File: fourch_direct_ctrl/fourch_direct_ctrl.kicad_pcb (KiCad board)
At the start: 4 copper layers, 72 x 72 mm, 53 parts, among them J1 Conn_01x04, J10 Conn_01x01, J11 Conn_01x01, J12 Conn_01x01, J13 Conn_01x01, J14 Conn_01x01, J15 Conn_01x01, J16 Conn_01x01, J17 Conn_01x01, J2 Conn_01x02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

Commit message: update silk
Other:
- board text added: "048ef97"
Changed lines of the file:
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@@
 		(layer "Edge.Cuts")
+	)
+	(gr_text "048ef97"
+		(at -35.5 3.5 -90)
+		(layer "F.SilkS")
+		(effects
+			(font
+				(size 1 1)
+				(thickness 0.15)
+			)
+			(justify left bottom)
+		)
 	)
 	(gr_text "GND"

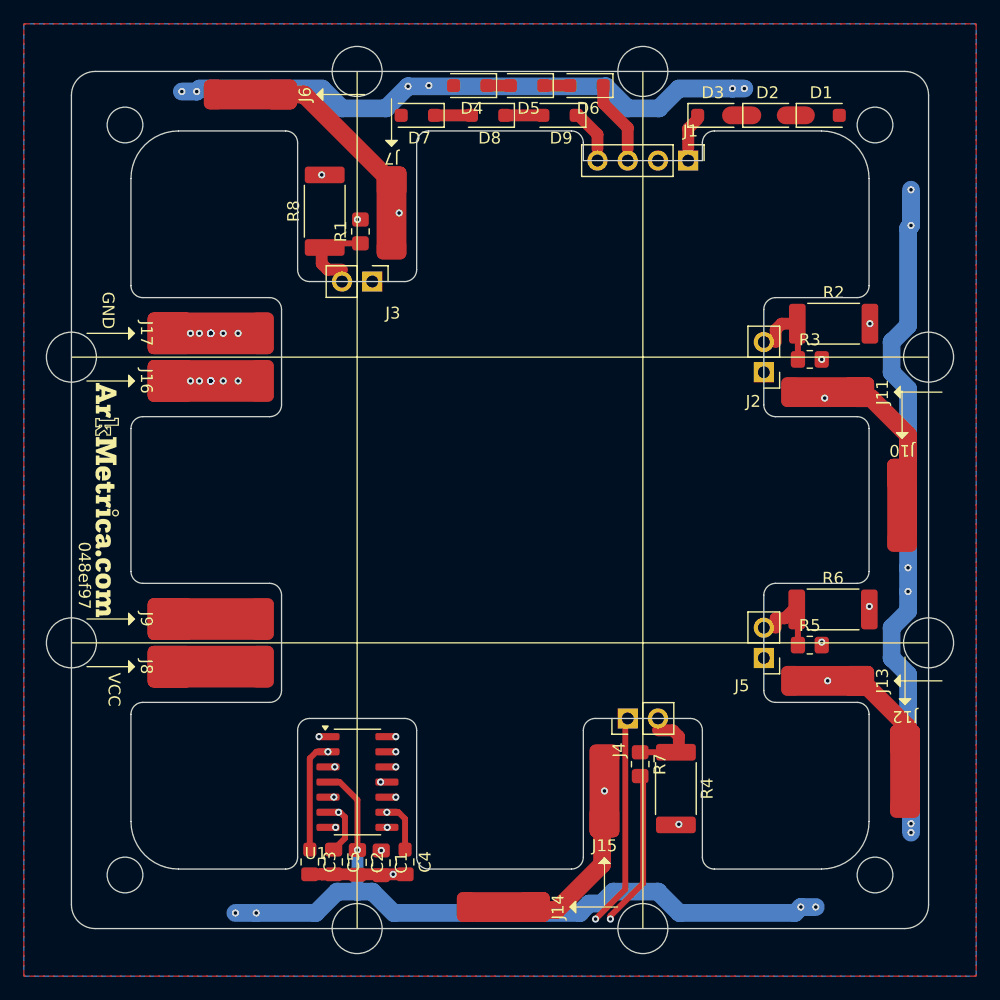
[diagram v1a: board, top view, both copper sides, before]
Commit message: rev up fourch lights, add distroboard
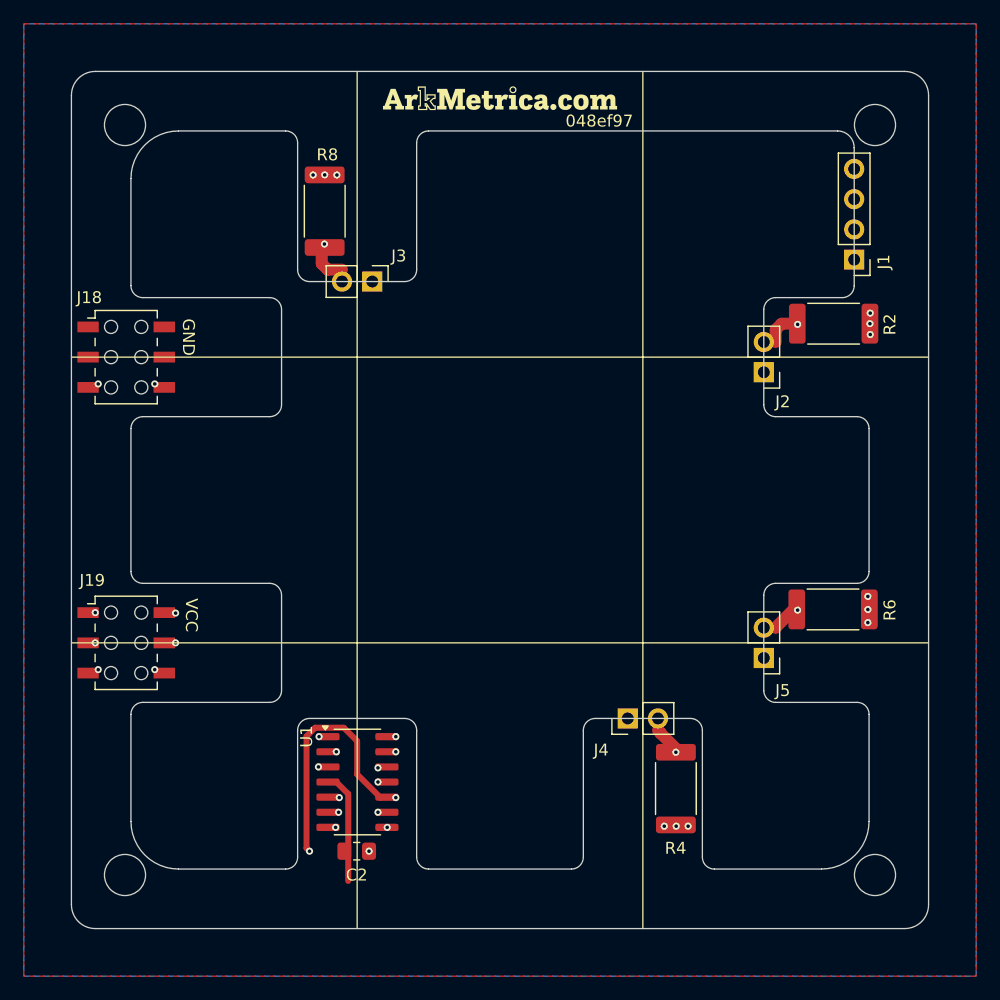
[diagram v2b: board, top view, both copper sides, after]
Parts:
- removed C1, C3, C4, C5: 1n, Capacitor_SMD:C_0805_2012Metric_Pad1.18x1.45mm_HandSolder
- removed D1, D2, D3, D4, D5, D6, D7, D8, D9: D, Diode_SMD:D_SOD-123F
- removed H10, H11, H12, H5, H6, H7, H8, H9: MountingHole, custom_footprints:MountingHole_4.2mm
- removed J10, J11, J12, J13, J14, J15, J6, J7: Conn_01x01, custom_footprints:TE_2834010-3_1x01_P3.0mm_Horizontal
- removed J16, J17, J8, J9: Conn_01x01, custom_footprints:TE_2834012-3_1x01_P4.0mm_Horizontal
- removed R1, R3, R5, R7: 2k2, Resistor_SMD:R_0805_2012Metric_Pad1.20x1.40mm_HandSolder
- added J18: Conn_02x03_Odd_Even, Connector_Wuerth:Wuerth_WR-PHD_610006243021_SMD_2x03_P2.54mm_Vertical, F.Cu at (-31.4, -12.0)
- added J19: Conn_02x03_Odd_Even, Connector_Wuerth:Wuerth_WR-PHD_610006243021_SMD_2x03_P2.54mm_Vertical, F.Cu at (-31.4, 12.0)
- H1, H2, H3, H4: footprint custom_footprints:MountingHole_3.0mm -> custom_footprints:MountingHole_3.45mm
- moved SYM1 47.2 mm to (0.00, -33.8), turned to 0 degrees
- moved J1 16.2 mm to (29.8, -20.2), turned to 180 degrees
- moved C2 0.94 mm to (-12.0, 29.5), turned to 0 degrees
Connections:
- J1 pad 1: Net-(D3-K) -> VCC
- J1 pad 3: Net-(D6-K) -> VCC
- J1 pad 4: Net-(D9-K) -> VCC
- U1 pad 13: Net-(U1D--) -> Net-(J3-Pin_2)
- U1 pad 2: Net-(U1A--) -> Net-(J2-Pin_2)
- U1 pad 6: Net-(U1B--) -> Net-(J4-Pin_2)
- U1 pad 9: Net-(U1C--) -> Net-(J5-Pin_2)
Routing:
- net VCC: track 169.5 -> 9.43 mm, vias 17 -> 0
- net Net-(U1D--): track 147.4 -> 0.00 mm, vias 3 -> 0
- net Net-(J3-Pin_2): track 6.42 -> 152.3 mm, vias 0 -> 2
- net Net-(U1A--): track 121.8 -> 0.00 mm, vias 2 -> 0
- net Net-(J2-Pin_2): track 6.08 -> 115.3 mm, vias 0 -> 2
- net Net-(J19-Pin_5): track 152.4 -> 63.6 mm
- net Net-(U1C--): track 83.7 -> 0.00 mm, vias 2 -> 0
- net Net-(J5-Pin_2): track 6.01 -> 84.9 mm, vias 0 -> 2
- net Net-(U1B--): track 47.2 -> 0.00 mm, vias 2 -> 0
- net Net-(J4-Pin_2): track 6.27 -> 46.0 mm, vias 0 -> 2
- net Net-(J18-Pin_6): track 115.3 -> 82.2 mm
- net Net-(J18-Pin_5): track 78.4 -> 96.4 mm, vias 2 -> 3
- net GND: track 9.00 -> 0.00 mm, vias 25 -> 18
- net Net-(J19-Pin_6): track 48.6 -> 55.2 mm
- net Net-(D6-K): track 6.15 -> 0.00 mm
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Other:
- outline, holes or cut-outs redrawn

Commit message: update silk
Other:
- board text added: "3523217"
- board text removed: "048ef97"
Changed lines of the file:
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@@
 		(layer "Edge.Cuts")
 	)
-	(gr_text "048ef97"
+	(gr_text "3523217"
 		(at 5.5 -31.25 0)
 		(layer "F.SilkS")

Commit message: minor touchups
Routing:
- net Net-(J3-Pin_2): track 152.3 -> 148.9 mm
- net Net-(J2-Pin_2): track 115.3 -> 112.2 mm
- net Net-(J5-Pin_2): track 84.9 -> 82.2 mm
- net Net-(J4-Pin_2): track 46.0 -> 43.4 mm
- net Net-(J18-Pin_5): track 96.4 -> 95.1 mm, vias 3 -> 2
- added copper zone on F.Cu, net Net-(J2-Pin_2)
- added copper zone on F.Cu, net Net-(J3-Pin_2)
- added copper zone on F.Cu, net Net-(J4-Pin_2)
- added copper zone on F.Cu, net Net-(J5-Pin_2)

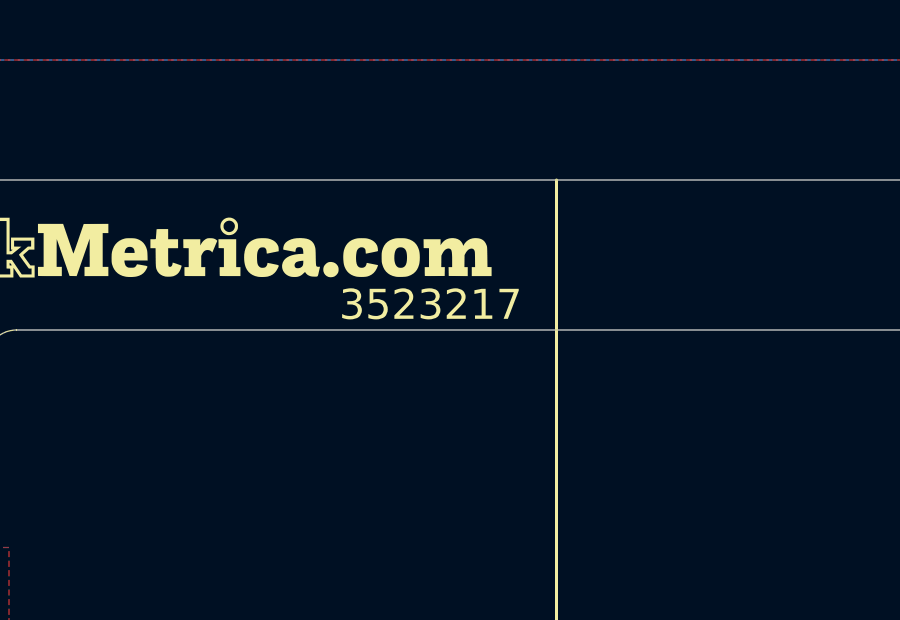
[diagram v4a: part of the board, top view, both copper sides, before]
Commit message: fillet corners
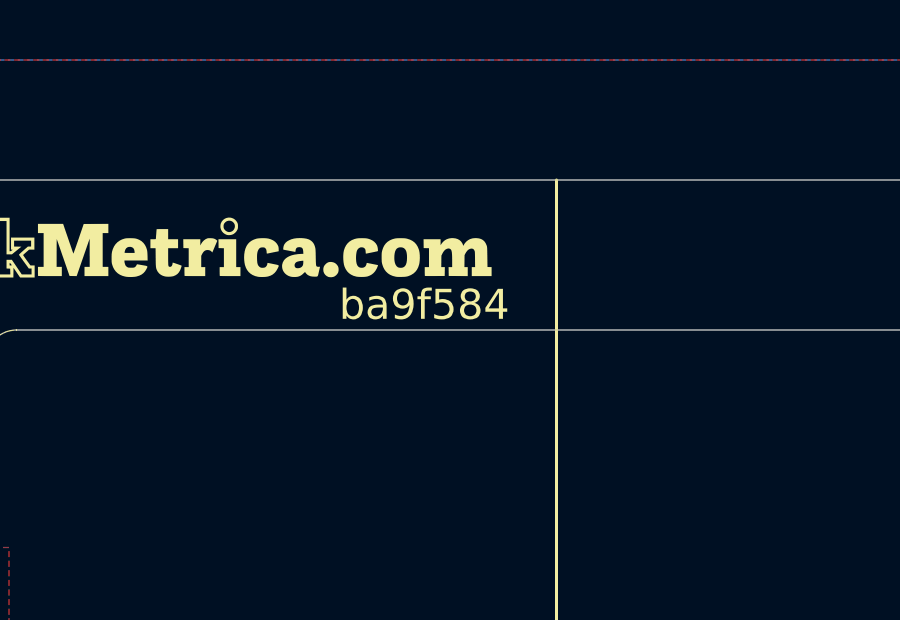
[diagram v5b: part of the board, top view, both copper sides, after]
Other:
- board text added: "ba9f584"
- board text removed: "3523217"
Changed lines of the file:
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@@
 		(layer "Edge.Cuts")
 	)
-	(gr_text "3523217"
+	(gr_text "ba9f584"
 		(at 4.75 -31.25 0)
 		(layer "F.SilkS")

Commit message: update silk
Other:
- board text added: "ab0086a"
- board text removed: "ba9f584"
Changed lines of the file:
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@@
 		(layer "Edge.Cuts")
 	)
-	(gr_text "ba9f584"
+	(gr_text "ab0086a"
 		(at 4.75 -31.25 0)
 		(layer "F.SilkS")

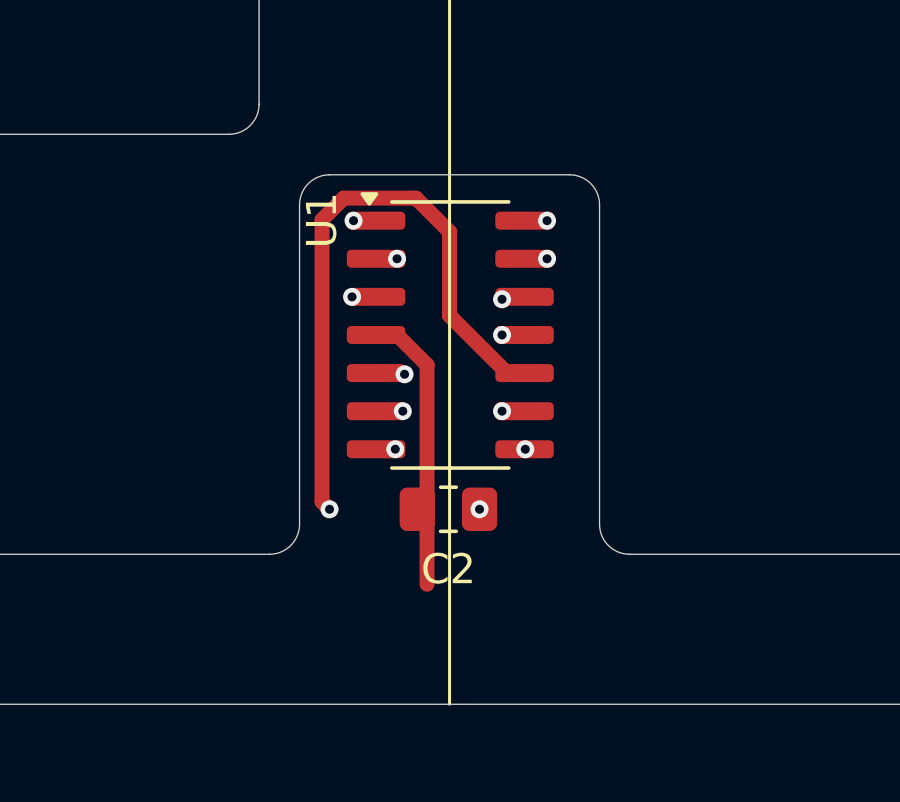
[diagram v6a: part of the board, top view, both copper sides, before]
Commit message: switch opamps to dual flavors, build in on-board TEC current control
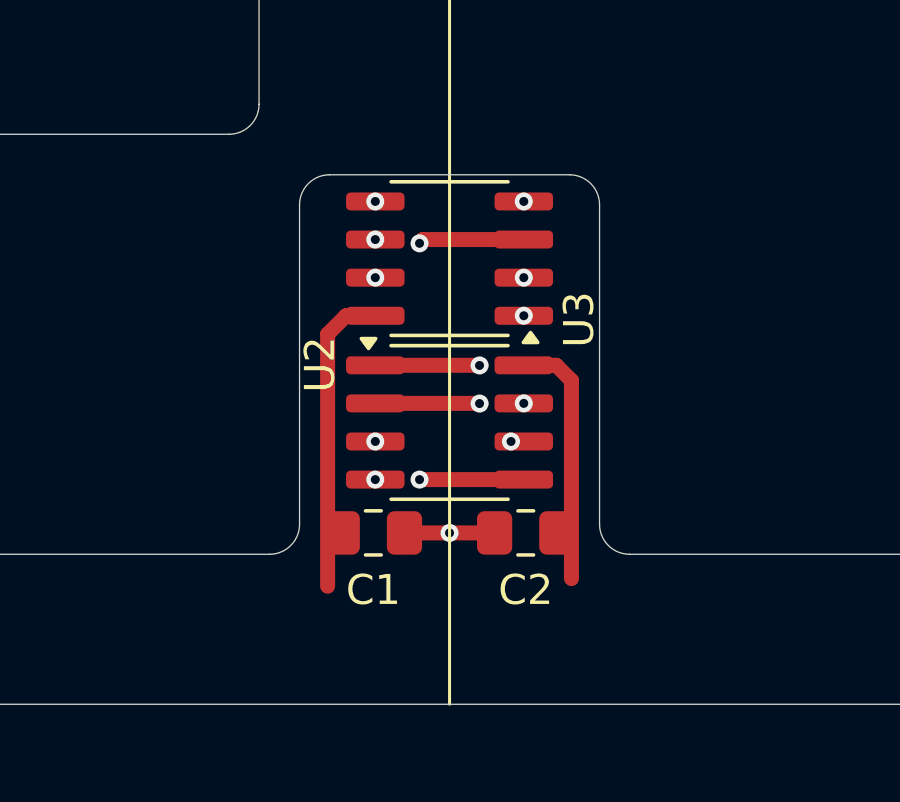
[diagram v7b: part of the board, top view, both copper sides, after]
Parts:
- removed U1: OPA4196xD, Package_SO:SOIC-14_3.9x8.7mm_P1.27mm
- added C1: 100n, Capacitor_SMD:C_0805_2012Metric_Pad1.18x1.45mm_HandSolder, F.Cu at (-14.5, 30.3)
- added U2: OPA2994xD, Package_SO:SOIC-8_3.9x4.9mm_P1.27mm, F.Cu at (-12.0, 26.6)
- added U3: OPA2994xD, Package_SO:SOIC-8_3.9x4.9mm_P1.27mm, F.Cu at (-12.0, 21.1)
- moved C2 2.70 mm to (-9.46, 30.3), turned to 180 degrees
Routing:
- net Net-(J18-Pin_5): track 95.1 -> 80.7 mm
- net Net-(J4-Pin_1): track 50.4 -> 38.8 mm
- net VCC: track 9.43 -> 18.6 mm
- net Net-(J3-Pin_2): track 148.9 -> 140.0 mm
- net Net-(J19-Pin_6): track 55.2 -> 63.8 mm
- net Net-(J18-Pin_6): track 82.2 -> 76.0 mm
- net Net-(J3-Pin_1): track 146.1 -> 142.1 mm
- net Net-(J2-Pin_1): track 112.2 -> 108.8 mm
- net GND: track 0.00 -> 3.00 mm, vias 18 -> 19
- net Net-(J5-Pin_1): track 76.7 -> 78.3 mm
- net Net-(J19-Pin_5): track 63.6 -> 62.4 mm
- net Net-(J5-Pin_2): track 82.2 -> 81.3 mm
- net Net-(J2-Pin_2): track 112.2 -> 111.4 mm

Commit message: update silk
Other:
- board text added: "ee118a9"
- board text removed: "ab0086a"
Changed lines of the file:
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@@
 		(layer "Edge.Cuts")
 	)
-	(gr_text "ab0086a"
+	(gr_text "ee118a9"
 		(at 4.75 -31.25 0)
 		(layer "F.SilkS")
